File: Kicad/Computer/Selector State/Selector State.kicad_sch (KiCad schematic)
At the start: 40 parts

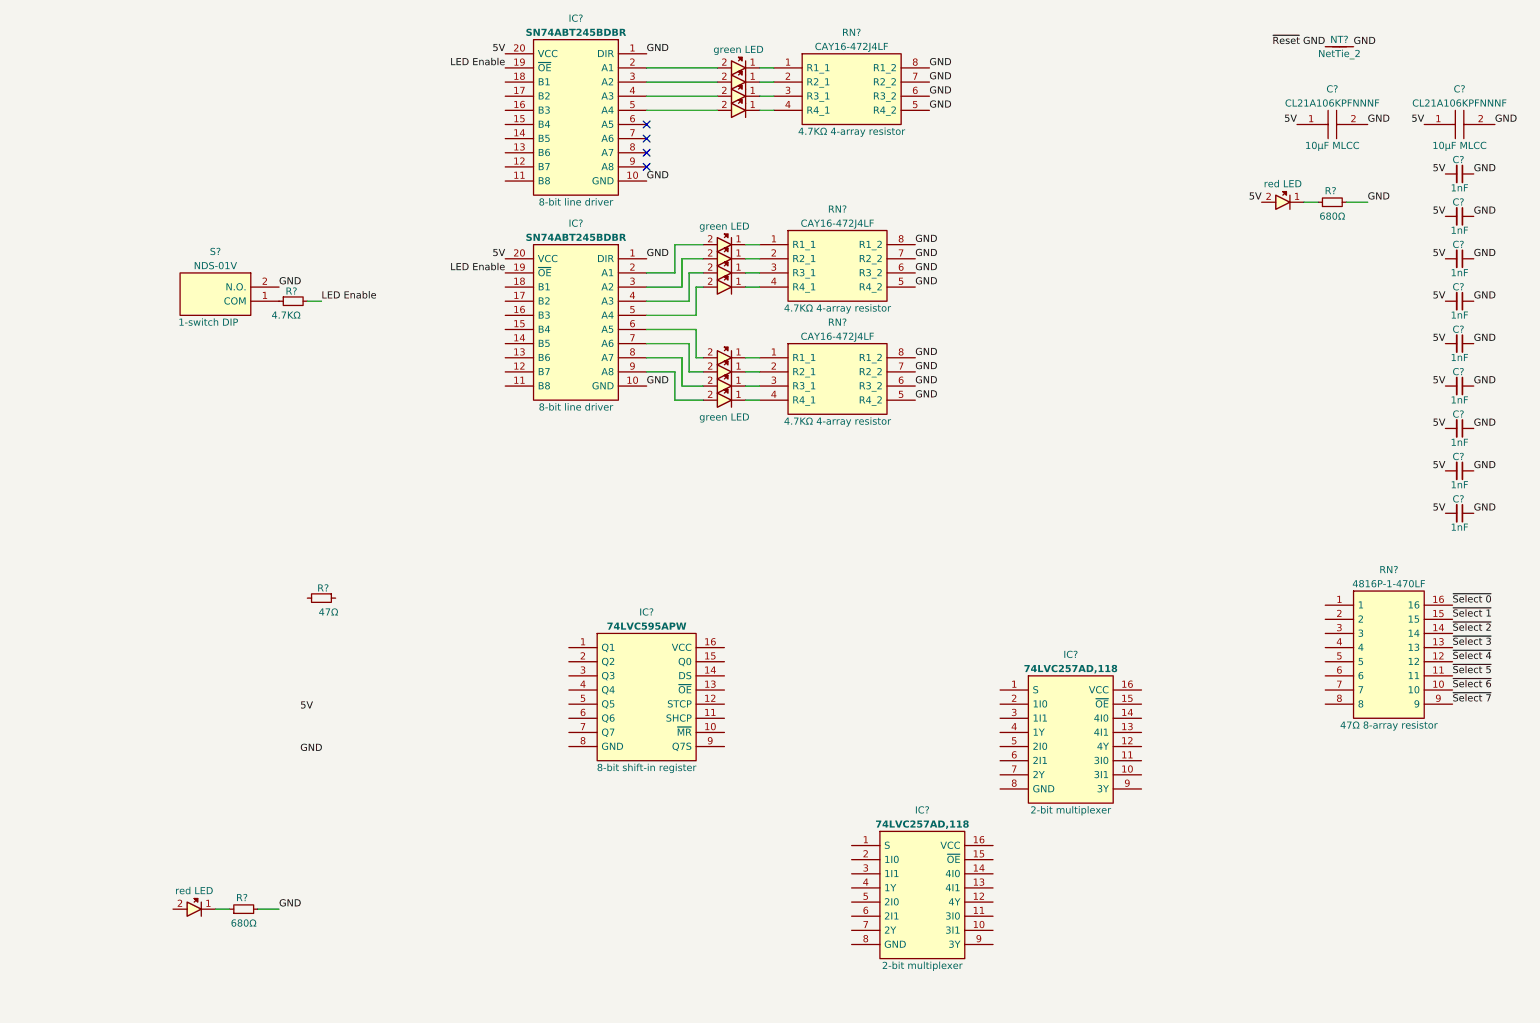
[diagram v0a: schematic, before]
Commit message: Updated logic gates with pretty symbols.
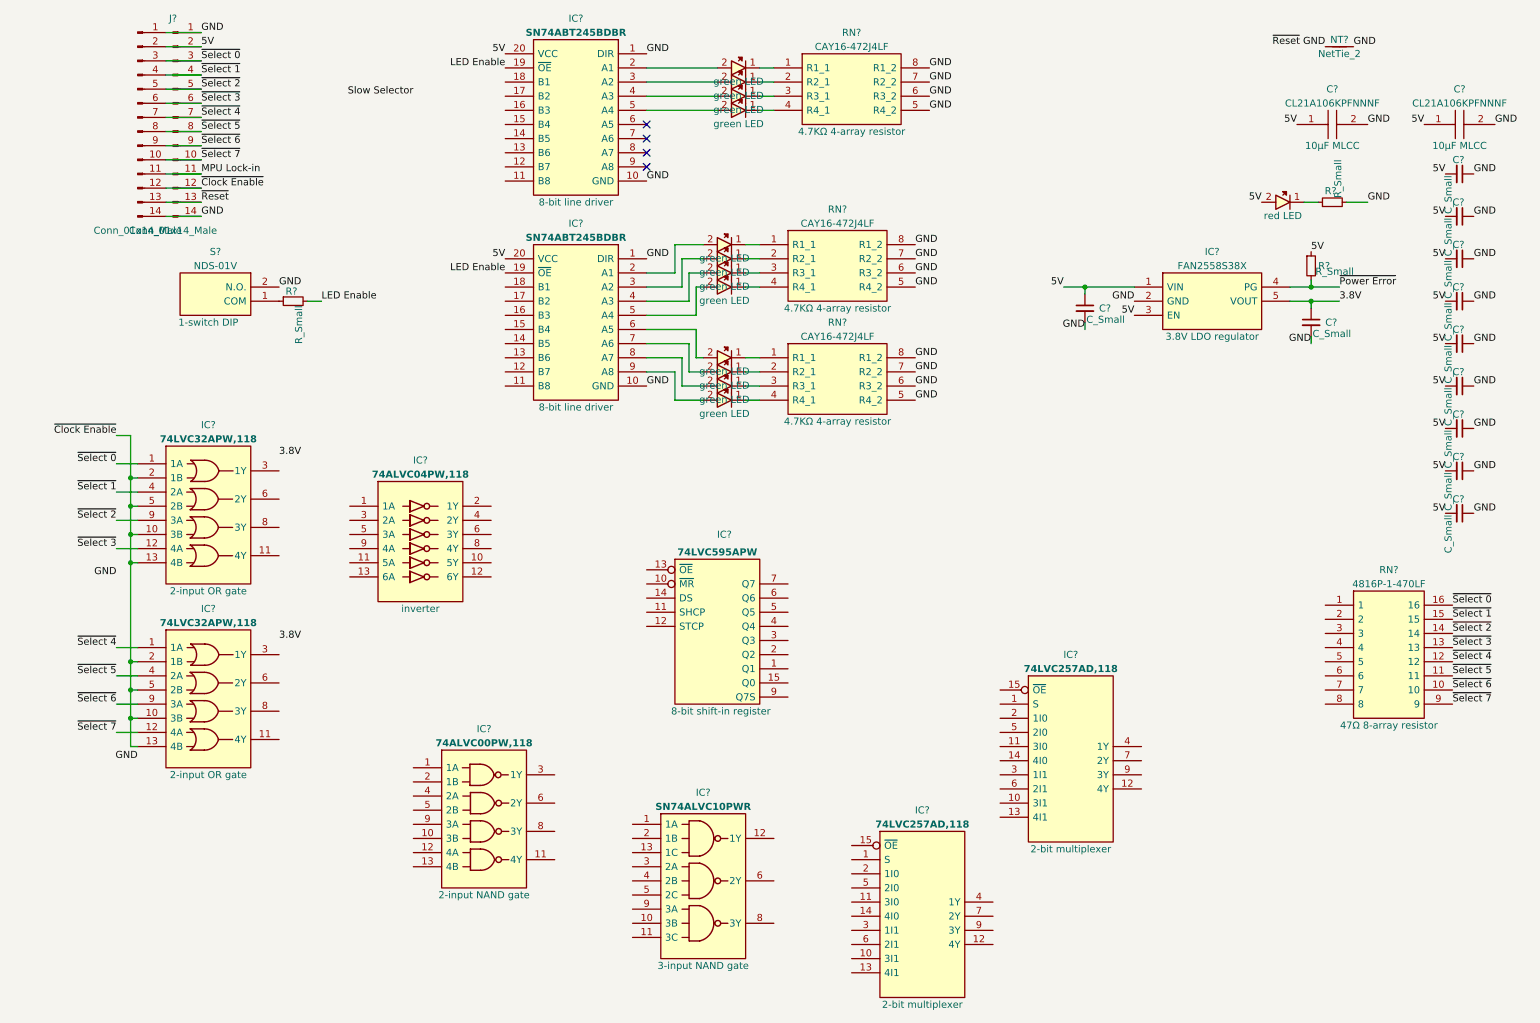
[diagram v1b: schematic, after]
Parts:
- removed LED?: 150224SS73100, LEDM2314X131N, symbol Wurth_Elektronik:150224SS73100
- removed R? (x2): R_Small, Resistor_SMD:R_0805_2012Metric, symbol Device:R_Small
- added C? (x2): C_Small, symbol Device:C_Small
- added IC?: 74ALVC04PW,118, SOP65P640X110-14N, symbol Nexperia:74ALVC04PW,118
- added IC? (x2): 74LVC32APW,118, SOP65P640X110-14N, symbol Nexperia:74LVC32APW,118
- added IC?: FAN2558S38X, SOT95P270X145-5N, symbol ON_Semiconductor:FAN2558S38X
- added IC?: 74ALVC00PW,118, SOP65P640X110-14N, symbol Nexperia:74ALVC00PW,118
- added IC?: SN74ALVC10PWR, SOP65P640X120-14N, symbol Texas_Instruments:SN74ALVC10PWR
- added J? (x2): Conn_01x14_Male, symbol Connector:Conn_01x14_Male
- added R?: R_Small, symbol Device:R_Small
- C? (x9): footprint Capacitor_SMD:C_0805_2012Metric -> (none)
- NT?: footprint NetTie:NetTie-2_SMD_Pad0.5mm -> (none)
- R?: footprint Resistor_SMD:R_0805_2012Metric -> (none); Resistance 680Ω -> (none)
- R?: footprint Resistor_SMD:R_0805_2012Metric -> (none); Resistance 4.7KΩ -> (none)
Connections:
- net 5V: now also C?.1, IC?.1 (VIN), IC?.3 (EN), J?.2 (Pin_2), J?.2 (Pin_2), R?.1
- net GND: now also IC?.8 (GND), IC?.8 (GND), IC?.8 (GND), C?.2, C?.2, IC?.2 (GND), IC?.7 (GND), IC?.7 (GND), IC?.7 (GND), IC?.7 (GND), IC?.7 (GND), J?.1 (Pin_1), J?.1 (Pin_1), J?.14 (Pin_14), J?.14 (Pin_14)
- net ~{Select 0}: now also IC?.1 (1A), J?.3 (Pin_3), J?.3 (Pin_3)
- net ~{Select 1}: now also IC?.4 (2A), J?.4 (Pin_4), J?.4 (Pin_4)
- net ~{Select 2}: now also IC?.9 (3A), J?.5 (Pin_5), J?.5 (Pin_5)
- net ~{Select 3}: now also IC?.12 (4A), J?.6 (Pin_6), J?.6 (Pin_6)
- net ~{Select 4}: now also IC?.1 (1A), J?.7 (Pin_7), J?.7 (Pin_7)
- net ~{Select 5}: now also IC?.4 (2A), J?.8 (Pin_8), J?.8 (Pin_8)
- net ~{Select 6}: now also IC?.9 (3A), J?.9 (Pin_9), J?.9 (Pin_9)
- net ~{Select 7}: now also IC?.12 (4A), J?.10 (Pin_10), J?.10 (Pin_10)
- net VCC: now reaches IC?.16 (VCC)
- net VCC: now also IC?.16 (VCC), IC?.16 (VCC), C?.1, IC?.14 (VCC), IC?.14 (VCC), IC?.14 (VCC), IC?.14 (VCC), IC?.14 (VCC), IC?.5 (VOUT)
- new net MPU Lock-in: J?.11 (Pin_11), J?.11 (Pin_11)
- new net ~{Clock Enable}: IC?.10 (3B), IC?.10 (3B), IC?.13 (4B), IC?.13 (4B), IC?.2 (1B), IC?.2 (1B), IC?.5 (2B), IC?.5 (2B), J?.12 (Pin_12), J?.12 (Pin_12)
- new net ~{Power Error}: IC?.4 (PG), R?.2
- new net ~{Reset}: J?.13 (Pin_13), J?.13 (Pin_13)

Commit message: Cleaning up the Select LDO.
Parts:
- removed C? (x11): C_Small, symbol Device:C_Small
- removed C? (x2): CL21A106KPFNNNF, CAPC2012X135N, symbol Samsung:CL21A106KPFNNNF
- removed LED?: 150224SS73100, LEDM2314X131N, symbol Wurth_Elektronik:150224SS73100
- removed NT?: NetTie_2, symbol Device:NetTie_2
- removed R? (x3): R_Small, symbol Device:R_Small
- removed RN? (x3): CAY16-472J4LF, CAY16472J4LF, symbol Bourns:CAY16-472J4LF
- removed S?: NDS-01V, NDS01V, symbol Apem:NDS-01V
- added C? (x14): C_Small, Capacitor_SMD:C_0805_2012Metric, symbol Device:C_Small
- added LD? (x2): 150224SS73100, SamacSys_Parts:150224SS73100A, symbol Wurth_Elektronik:150224SS73100
- added NT?: NetTie_2, NetTie:NetTie-2_SMD_Pad0.5mm, symbol Device:NetTie_2
- added R?: R_Small, Resistor_SMD:R_0805_2012Metric, symbol Device:R_Small
- added RN? (x3): CAY16-681J4LF, SamacSys_Parts:CAY16-J4, symbol Bourns:CAY16-681J4LF
- added RN?: CAY16-102J4LF, SamacSys_Parts:CAY16-J4, symbol Bourns:CAY16-102J4LF
- J? (x2): footprint (none) -> Connector_PinHeader_2.54mm:PinHeader_1x14_P2.54mm_Vertical
- LED? (x12): Silkscreen (none) -> grn
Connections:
- net GND: now also C?.1, C?.1, C?.1, C?.1, C?.1, C?.1, C?.1, C?.1, C?.1, C?.1, C?.1, C?.1, C?.1, C?.1, RN?.1 (R1), RN?.3 (R3), RN?.4 (R4), RN?.5 (R4), RN?.5 (R4), RN?.5 (R4), RN?.6 (R3), RN?.6 (R3), RN?.6 (R3), RN?.7 (R2), RN?.7 (R2), RN?.7 (R2), RN?.8 (R1), RN?.8 (R1), RN?.8 (R1); no longer IC?.1 (DIR), IC?.1 (DIR)
- net VCC: now also IC?.1 (DIR), IC?.1 (DIR), IC?.20 (VCC), IC?.20 (VCC), J?.2 (Pin_2), J?.2 (Pin_2), C?.2, C?.2, C?.2, C?.2, C?.2, C?.2, C?.2, C?.2, C?.2, C?.2, C?.2, C?.2, C?.2, NT?.1, R?.2
- net ~{Power Error}: now also R?.1
- net at LED?.1: now also RN?.2 (R2) (x3)
- net at LED?.2: now also IC?.13 (B6); no longer IC?.7 (A6)
- net at LED?.1: now also RN?.1 (R1) (x3)
- net at LED?.1: now also RN?.3 (R3) (x3)
- net at LED?.1: now also RN?.4 (R4) (x3)
- net at LED?.2: now also IC?.18 (B1); no longer IC?.2 (A1)
- net at LED?.2: now also IC?.17 (B2); no longer IC?.3 (A2)
- net at LED?.2: now also IC?.15 (B4); no longer IC?.5 (A4)
- net at IC?.11 (B8): now also LED?.2
- net at IC?.12 (B7): now also LED?.2
- net at IC?.14 (B5): now also LED?.2
- net at IC?.16 (B3): now also LED?.2 (x2)
- net at IC?.18 (B1): now also LED?.2
- net at IC?.2 (A1): no longer LED?.2
- net at IC?.4 (A3): no longer LED?.2 (x2)
- net at IC?.6 (A5): no longer LED?.2
- net at IC?.8 (A7): no longer LED?.2
- net at IC?.9 (A8): no longer LED?.2
- net at IC?.15 (B4): now also LED?.2
- net at IC?.17 (B2): now also LED?.2
- net at IC?.3 (A2): no longer LED?.2
- net at IC?.5 (A4): no longer LED?.2
- removed net 5V: IC?.1 (VIN), IC?.20 (VCC), IC?.20 (VCC), IC?.3 (EN), J?.2 (Pin_2), J?.2 (Pin_2)
- new net: LD?.1, RN?.8 (R1)
- new net: LD?.1, RN?.6 (R3)
- new net Power LED: LD?.2, NT?.2
- new net Reset LED: LD?.2
- new net Source 5V: C?.2, IC?.1 (VIN), IC?.3 (EN)
- no-connect marks 4 -> 6
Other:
- moved on the sheet: IC?

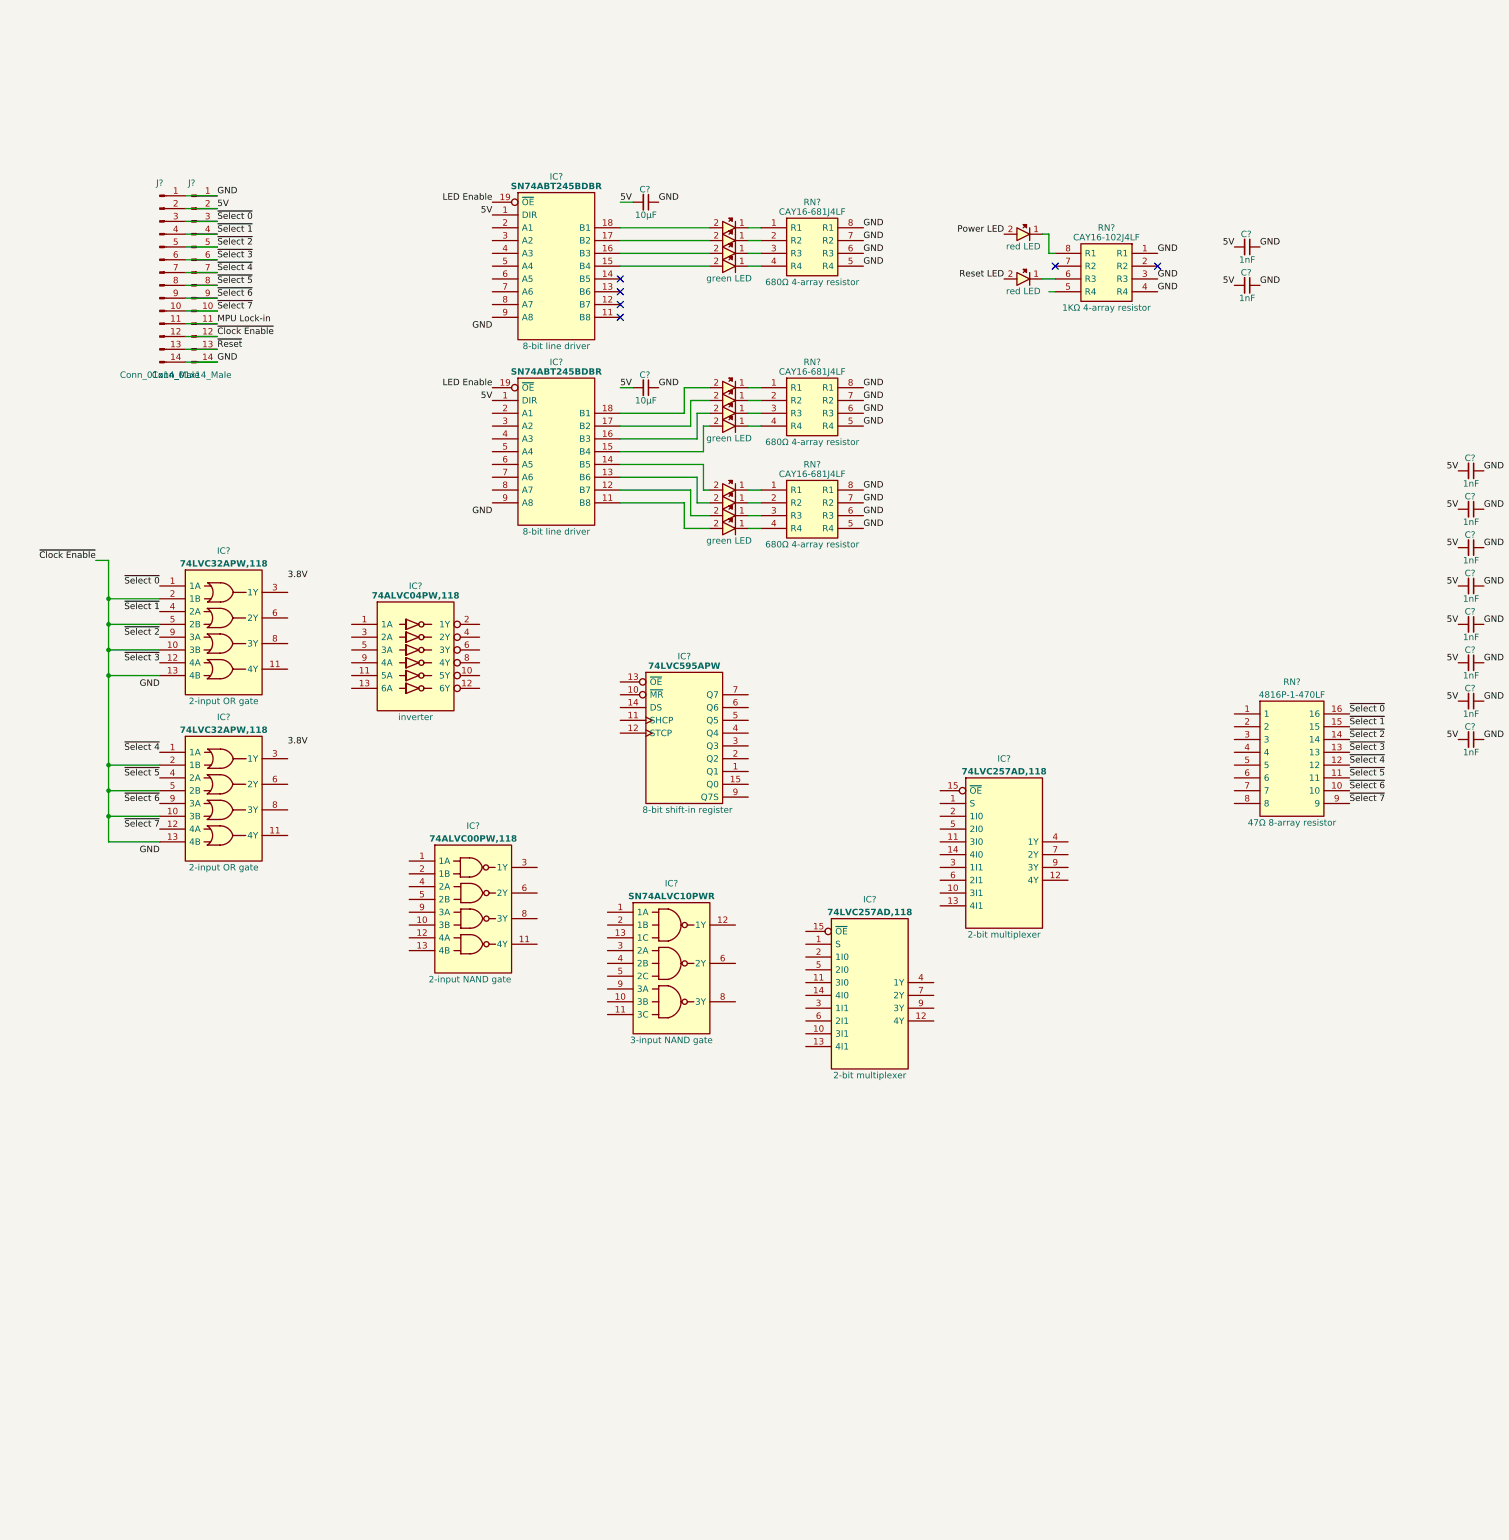
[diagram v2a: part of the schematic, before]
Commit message: Removed 'Logisim appeasing' bus transceiver.
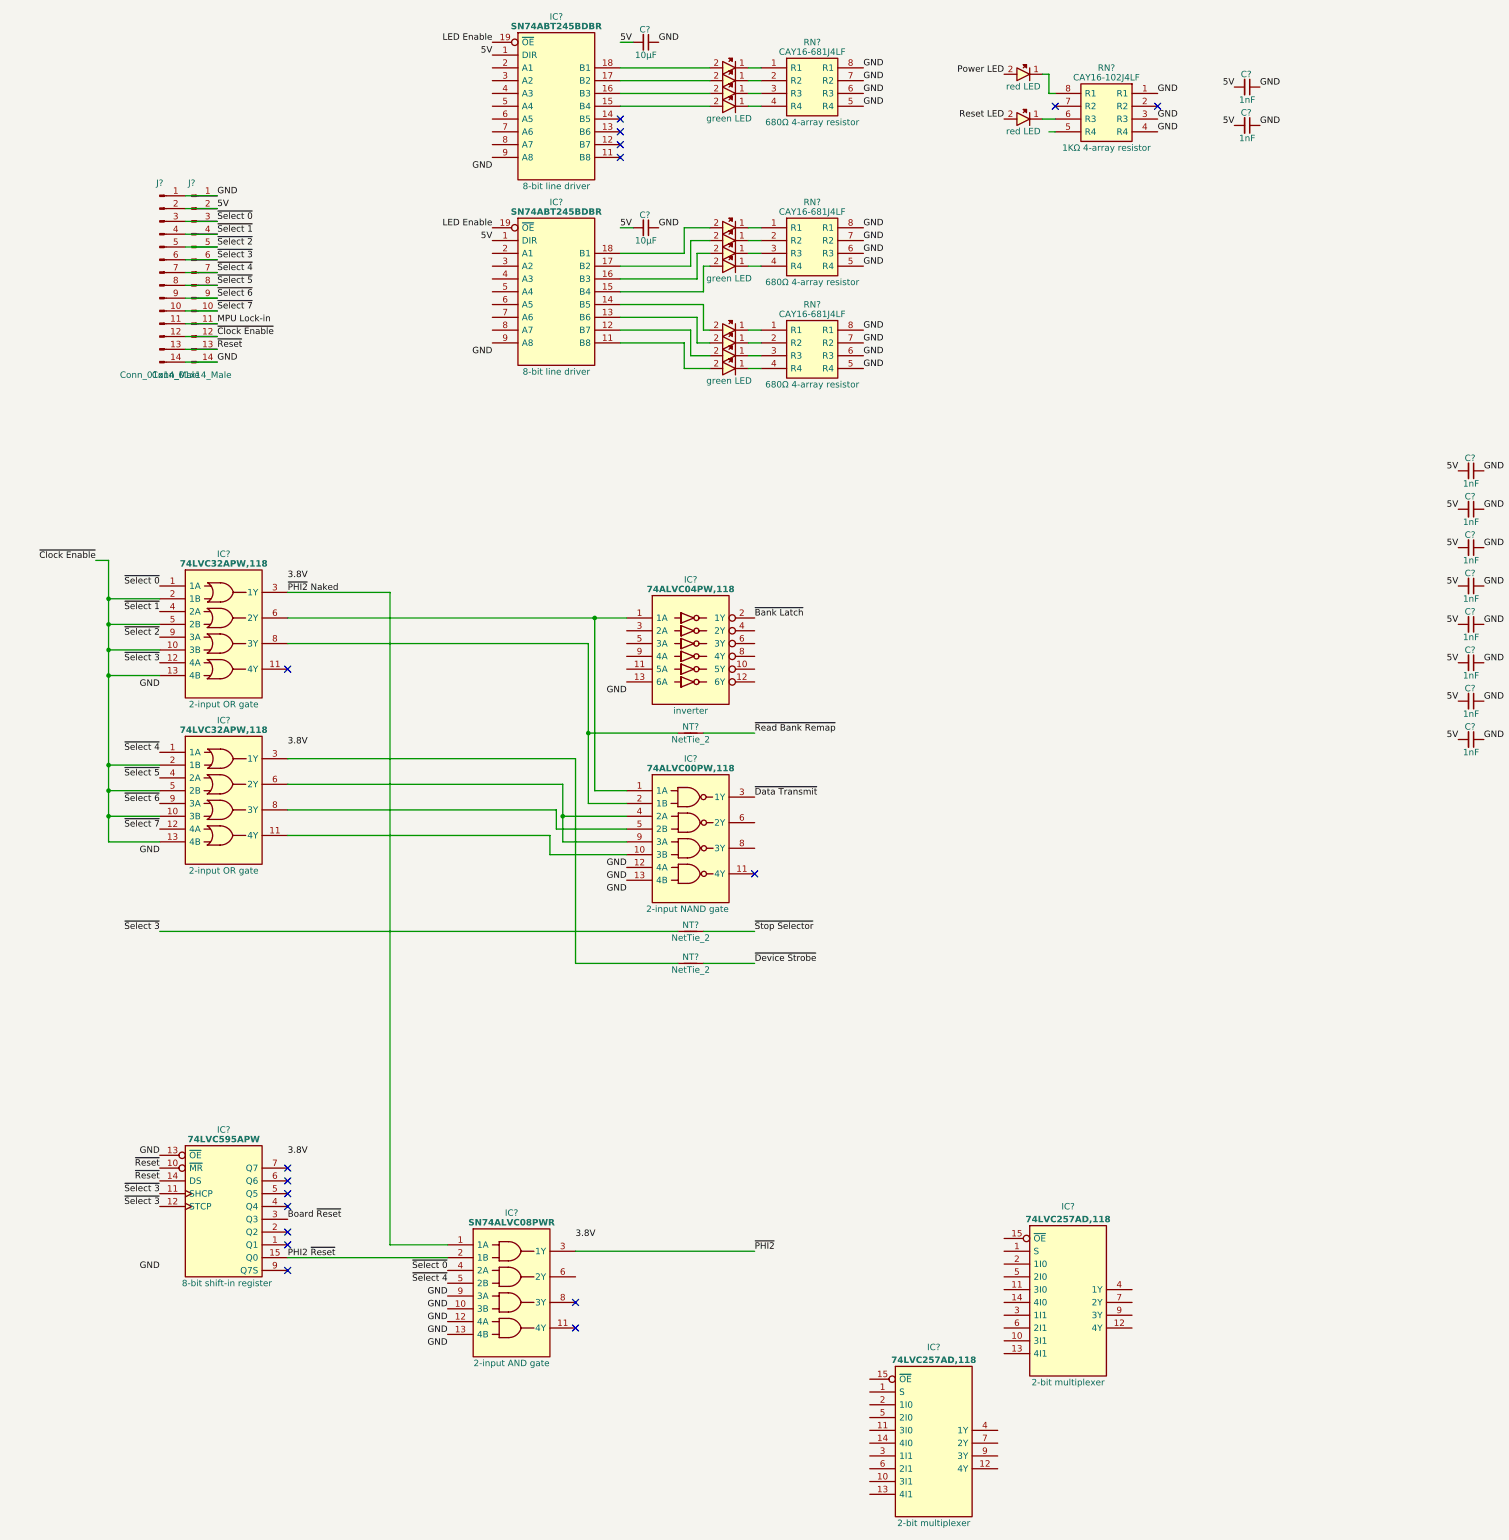
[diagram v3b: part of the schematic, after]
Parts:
- removed IC?: 74ALVC00PW,118, SOP65P640X110-14N, symbol Nexperia:74ALVC00PW,118
- removed IC?: SN74ALVC10PWR, SOP65P640X120-14N, symbol Texas_Instruments:SN74ALVC10PWR
- removed RN?: 4816P-1-470LF, SOIC127P762X240-16N, symbol Bourns:4816P-1-470LF
- added IC?: SN74ALVC08PWR, SOP65P640X120-14N, symbol Texas_Instruments:SN74ALVC08PWR
- added IC?: 74ALVC00PW,118, SOP65P640X110-14N, symbol Nexperia:74ALVC00PW,118
- added NT? (x3): NetTie_2, NetTie:NetTie-2_SMD_Pad0.5mm, symbol Device:NetTie_2
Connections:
- net GND: now also IC?.13 (~{OE}), IC?.10 (3B), IC?.12 (4A), IC?.12 (4A), IC?.13 (4B), IC?.13 (4B), IC?.7 (GND), IC?.7 (GND), IC?.9 (3A)
- net VCC: now also IC?.14 (VCC), IC?.14 (VCC)
- net ~{Reset}: now also IC?.10 (~{MR}), IC?.14 (DS)
- net ~{Select 0}: now also IC?.4 (2A)
- net ~{Select 3}: now also IC?.11 (SHCP), IC?.12 (STCP), NT?.1
- net ~{Select 4}: now also IC?.5 (2B)
- net at IC?.1 (1A): now also IC?.6 (2Y), IC?.1 (1A)
- net ~{Bank Latch}: now reaches IC?.2 (1Y)
- net at IC?.11 (4Y): now also IC?.10 (3B)
- net at IC?.3 (1Y): now also NT?.1
- net at IC?.6 (2Y): now also IC?.4 (2A), IC?.9 (3A)
- net at IC?.8 (3Y): now also IC?.5 (2B)
- net ~{PHI2} Naked: now reaches IC?.3 (1Y)
- net ~{PHI2} Naked: now also IC?.1 (1A)
- net at IC?.8 (3Y): now also IC?.2 (1B), NT?.1
- net PHI2 ~{Reset}: now reaches IC?.15 (Q0)
- net PHI2 ~{Reset}: now also IC?.2 (1B)
- net Board ~{Reset}: now reaches IC?.3 (Q3)
- new net ~{Data Transmit}: IC?.3 (1Y)
- new net ~{Device Strobe}: NT?.2
- new net ~{PHI2}: IC?.3 (1Y)
- new net ~{Read Bank Remap}: NT?.2
- new net ~{Stop Selector}: NT?.2
- no-connect marks 6 -> 17
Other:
- moved on the sheet: C?, IC?, RN?
